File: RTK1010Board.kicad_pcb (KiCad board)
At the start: 2 copper layers, 56.2 x 53.3 mm, 56 parts, among them J1 SMA, J2 IPEX, J3 USB_OTG, U1 RTK-1010, U2 MCP1700-3002E_SOT23, U3 MCP1700-3002E_SOT23, U4 ESP32-S2-WROVER

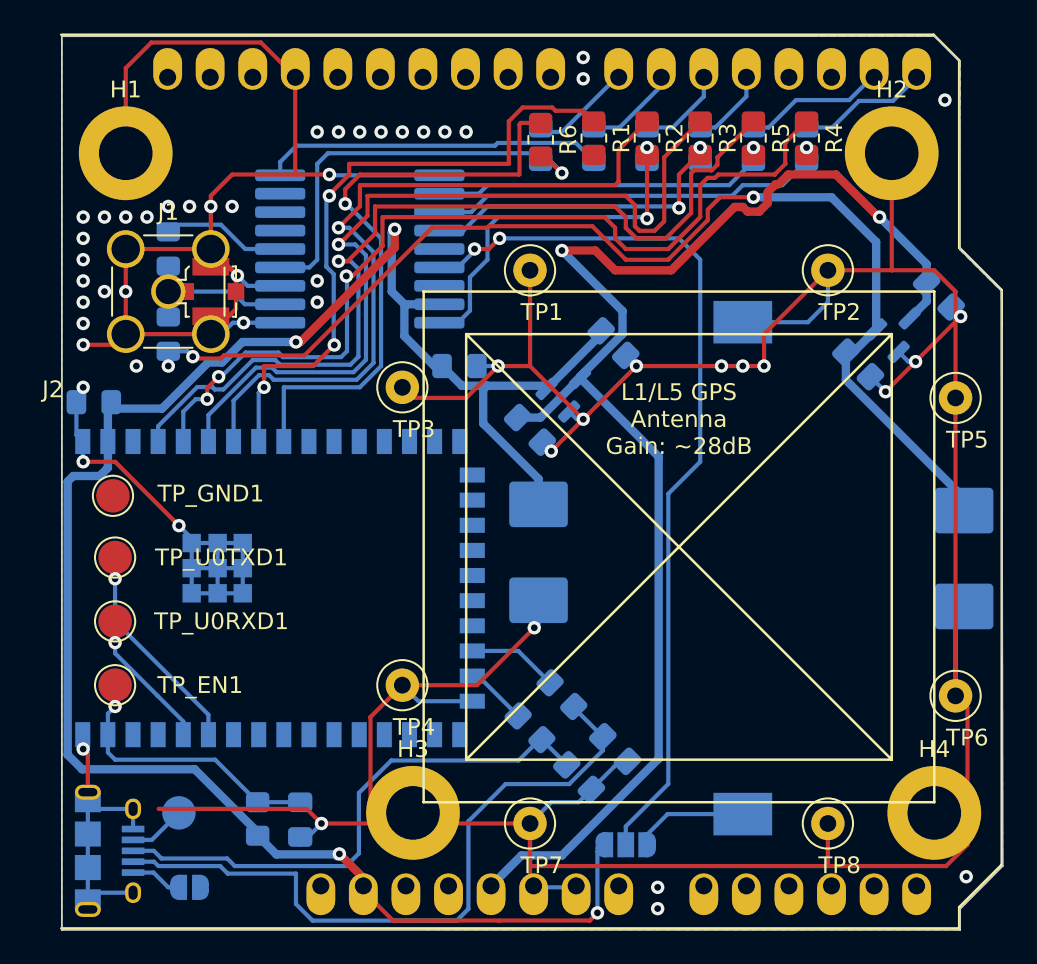
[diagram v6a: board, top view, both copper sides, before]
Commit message: bno055 added
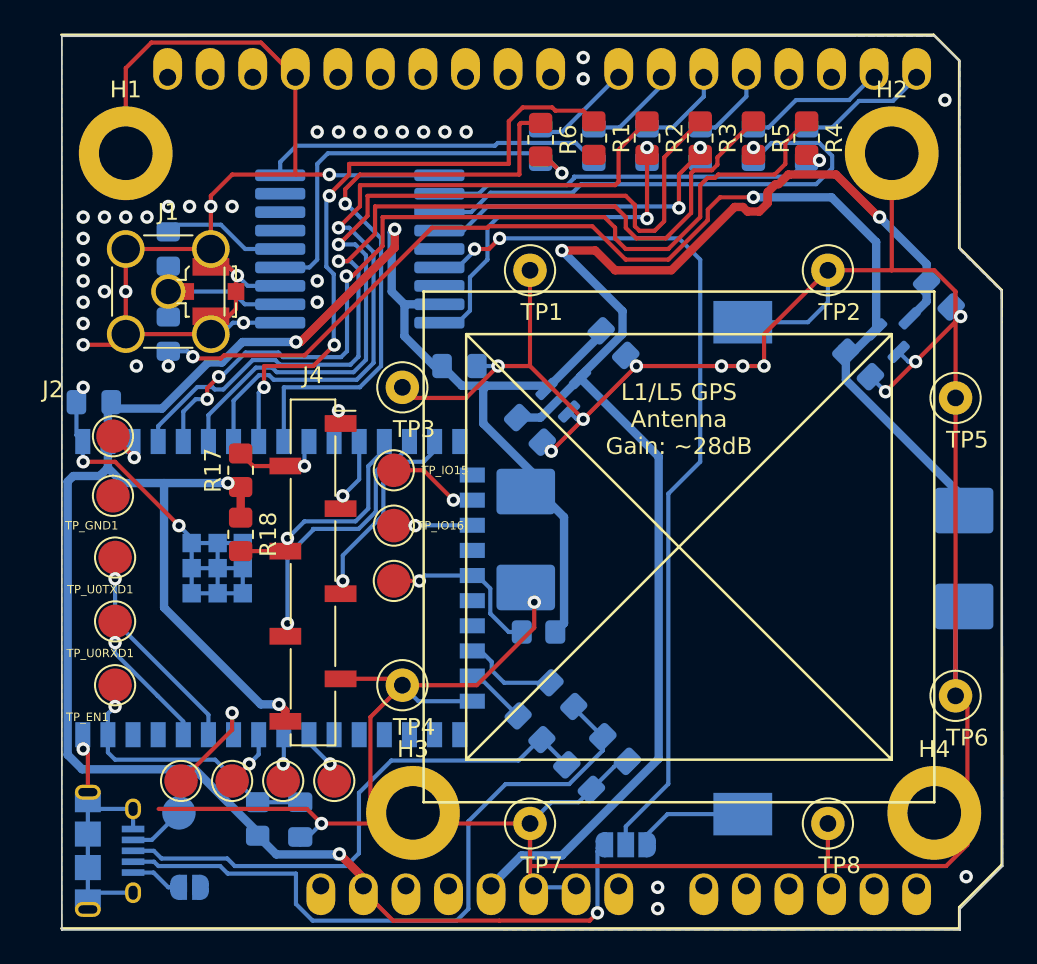
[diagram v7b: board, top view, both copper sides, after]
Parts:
- added J4: BNO055, Connector_PinSocket_2.54mm:PinSocket_1x08_P2.54mm_Vertical_SMD_Pin1Right, F.Cu at (186.4, 105.7)
- added R16: 10k, Resistor_SMD:R_0805_2012Metric_Pad1.20x1.40mm_HandSolder, B.Cu at (199.9, 109.2)
- added R17: 10k, Resistor_SMD:R_0805_2012Metric_Pad1.20x1.40mm_HandSolder, F.Cu at (182.1, 99.6)
- added R18: 10k, Resistor_SMD:R_0805_2012Metric_Pad1.20x1.40mm_HandSolder, F.Cu at (182.1, 103.4)
- added TP_BOOT1: TestPoint, TestPoint:TestPoint_Pad_D2.0mm, F.Cu at (174.5, 97.5)
- added TP_IO15: TestPoint, TestPoint:TestPoint_Pad_D2.0mm, F.Cu at (191.3, 99.6)
- added TP_IO16: TestPoint, TestPoint:TestPoint_Pad_D2.0mm, F.Cu at (191.3, 102.9)
- added TP_IO18: TestPoint, TestPoint:TestPoint_Pad_D2.0mm, F.Cu at (191.3, 106.2)
- added TP_IO39: TestPoint, TestPoint:TestPoint_Pad_D2.0mm, F.Cu at (187.7, 118.1)
- added TP_IO40: TestPoint, TestPoint:TestPoint_Pad_D2.0mm, F.Cu at (184.7, 118.1)
- added TP_IO41: TestPoint, TestPoint:TestPoint_Pad_D2.0mm, F.Cu at (181.6, 118.1)
- added TP_IO42: TestPoint, TestPoint:TestPoint_Pad_D2.0mm, F.Cu at (178.6, 118.1)
- moved C11 1.08 mm to (199.1, 103.7)
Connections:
- U1 pad 2: RX -> TX
- U1 pad 3: TX -> RX
- U4 pad 10: unconnected-(U4-Pad10) -> BNO_BOOT
- U4 pad 11: unconnected-(U4-Pad11) -> BNO_RESET
- U4 pad 12: unconnected-(U4-Pad12) -> BNO_INT
- U4 pad 13: unconnected-(U4-Pad13) -> BNO_ADDR
- U4 pad 14: unconnected-(U4-Pad14) -> BNO_RX
- U4 pad 15: unconnected-(U4-Pad15) -> BNO_TX
- U4 pad 18: unconnected-(U4-Pad18) -> Net-(TP_IO15-Pad1)
- U4 pad 19: unconnected-(U4-Pad19) -> Net-(TP_IO16-Pad1)
- U4 pad 21: unconnected-(U4-Pad21) -> Net-(R16-Pad2)
- U4 pad 3: unconnected-(U4-Pad3) -> Net-(TP_BOOT1-Pad1)
- U4 pad 33: unconnected-(U4-Pad33) -> Net-(TP_IO39-Pad1)
- U4 pad 34: unconnected-(U4-Pad34) -> Net-(TP_IO40-Pad1)
- U4 pad 35: unconnected-(U4-Pad35) -> Net-(TP_IO41-Pad1)
- U4 pad 36: unconnected-(U4-Pad36) -> Net-(TP_IO42-Pad1)
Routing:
- net +3V3: track 118.4 -> 155.7 mm, vias 4 -> 6
- net BNO_RX: track 0.00 -> 16.6 mm, vias 0 -> 1
- net BNO_ADDR: track 0.00 -> 13.4 mm, vias 0 -> 1
- net BNO_TX: track 0.00 -> 12.1 mm, vias 0 -> 1
- net RX: track 20.8 -> 32.0 mm
- net Net-(R16-Pad2): track 0.00 -> 10.0 mm, vias 0 -> 1
- net Net-(TP_IO42-Pad1): track 0.00 -> 6.67 mm, vias 0 -> 1
- net BNO_BOOT: track 0.00 -> 5.69 mm, vias 0 -> 1
- net Net-(TP_IO15-Pad1): track 0.00 -> 5.42 mm, vias 0 -> 1
- net Net-(TP_IO16-Pad1): track 0.00 -> 4.69 mm, vias 0 -> 1
- net BNO_INT: track 0.00 -> 4.46 mm, vias 0 -> 1
- net GND: track 335.2 -> 339.1 mm
- net Net-(TP_IO41-Pad1): track 0.00 -> 3.42 mm, vias 0 -> 1
- net Net-(TP_IO39-Pad1): track 0.00 -> 3.39 mm, vias 0 -> 1
- net Net-(TP_BOOT1-Pad1): track 0.00 -> 2.78 mm, vias 0 -> 1
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
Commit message: UART LoopIn option added USB connected to USB pins
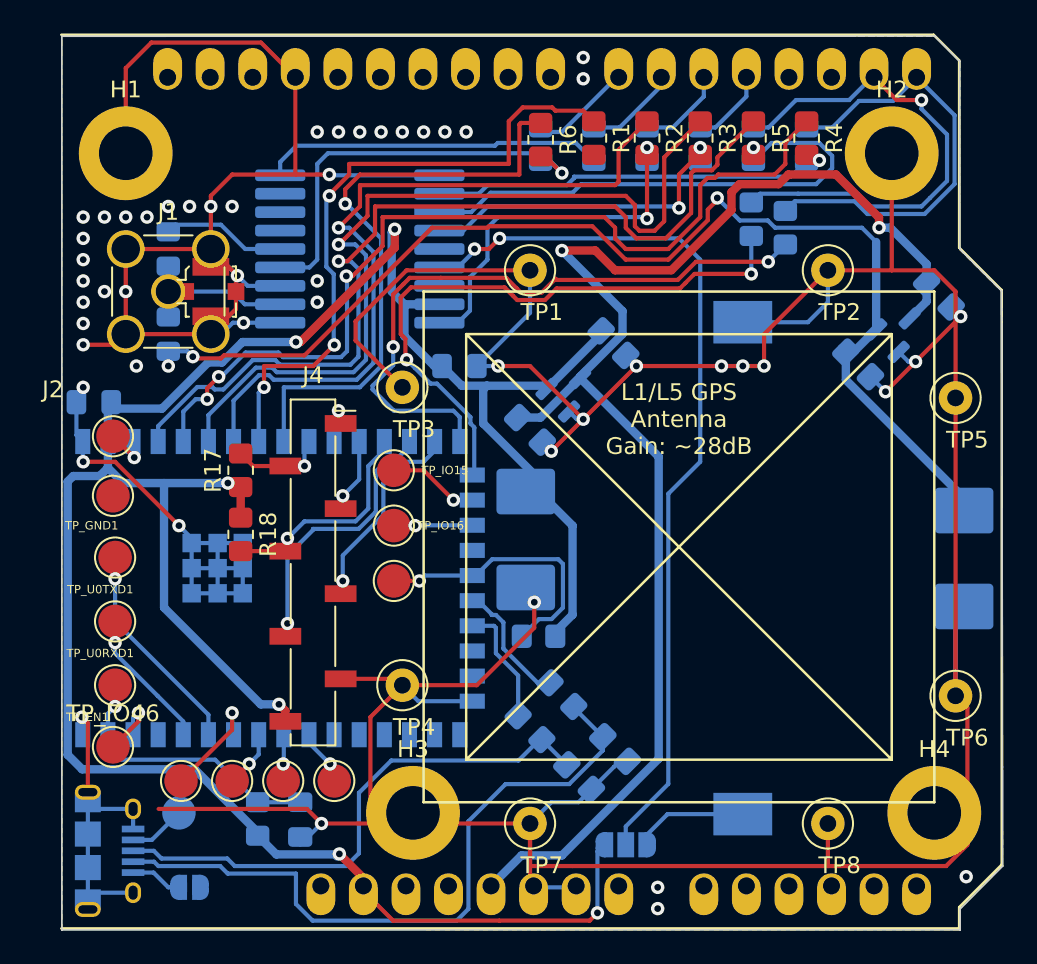
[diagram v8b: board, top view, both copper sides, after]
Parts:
- added R19: 100, Resistor_SMD:R_0805_2012Metric_Pad1.20x1.40mm_HandSolder, B.Cu at (214.6, 85.1)
- added R20: 100, Resistor_SMD:R_0805_2012Metric_Pad1.20x1.40mm_HandSolder, B.Cu at (212.6, 84.6)
- added TP_IO46: TestPoint, TestPoint:TestPoint_Pad_D2.0mm, F.Cu at (174.5, 116.1)
- moved R16 0.25 mm to (199.9, 109.5)
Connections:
- net /RXD renamed RXD
- net /TXD renamed TXD
- R13 pad 2: Net-(R13-Pad2) -> Net-(U4-Pad23)
- R14 pad 2: Net-(R14-Pad2) -> Net-(U4-Pad22)
- U4 pad 16: unconnected-(U4-Pad16) -> Net-(U4-Pad16)
- U4 pad 17: unconnected-(U4-Pad17) -> Net-(U4-Pad17)
- U4 pad 22: unconnected-(U4-Pad22) -> Net-(U4-Pad22)
- U4 pad 23: unconnected-(U4-Pad23) -> Net-(U4-Pad23)
- U4 pad 24: Net-(R14-Pad2) -> unconnected-(U4-Pad24)
- U4 pad 25: Net-(R13-Pad2) -> unconnected-(U4-Pad25)
- U4 pad 40: unconnected-(U4-Pad40) -> Net-(U4-Pad40)
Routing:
- net Net-(U4-Pad16): track 0.00 -> 39.0 mm, vias 0 -> 2
- net Net-(U4-Pad17): track 0.00 -> 37.1 mm, vias 0 -> 2
- net RXD: track 8.44 -> 30.1 mm, vias 0 -> 1
- net TXD: track 7.80 -> 26.5 mm
- net GND: track 339.1 -> 352.8 mm, vias 52 -> 51
- net Net-(U4-Pad22): track 0.00 -> 7.61 mm
- net Net-(U4-Pad23): track 0.00 -> 7.27 mm
- net Net-(R16-Pad2): track 10.0 -> 16.8 mm
- net Net-(R14-Pad2): track 5.73 -> 0.00 mm
- net Net-(R13-Pad2): track 4.15 -> 0.00 mm
- net Net-(U4-Pad40): track 0.00 -> 4.10 mm, vias 0 -> 1
